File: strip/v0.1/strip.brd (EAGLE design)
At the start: 67 x 12 mm, 102 parts, among them IC1 LP2992, IC2 ADP3110A-SO8, IC3 MAX3051, IC4 OPA335, IC5 ADP3110A-SO8, IC6 ADP3110A-SO8, IC7 STM32F050CX, Q1 IRF7828, Q2 IRF7828, Q3 IRF7828, Q4 IRF7828, Q5 IRF7828, Q6 IRF7828

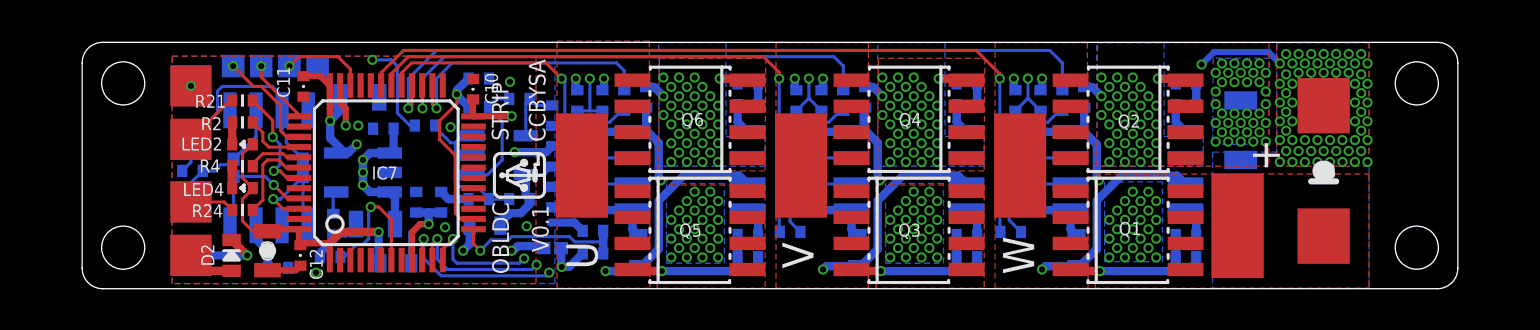
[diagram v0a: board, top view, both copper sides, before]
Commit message: Added tabs for panelization.
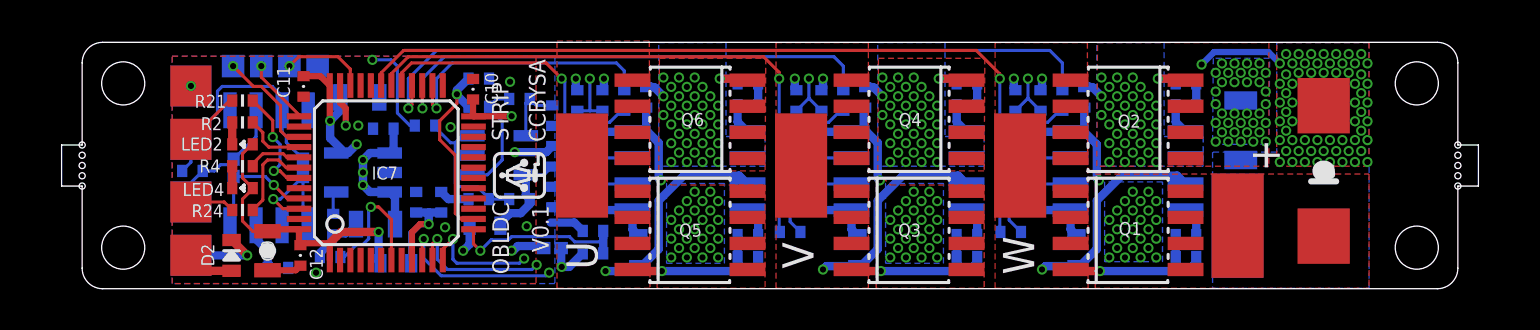
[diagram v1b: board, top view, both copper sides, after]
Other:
- board size 67 x 12 mm -> 69 x 12 mm
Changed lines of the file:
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@@
 <setting verticaltext="up"/>
 </settings>
-<grid distance="3" unitdist="mil" unit="mm" style="dots" multiple="1" display="yes" altdistance="0.5" altunitdist="mil" altunit="mil"/>
+<grid distance="0.5" unitdist="mm" unit="mm" style="dots" multiple="1" display="yes" altdistance="0.5" altunitdist="mil" altunit="mil"/>
 <layers>
 <layer number="1" name="Top" color="4" fill="1" visible="yes" active="yes"/>
@@
 <layer number="43" name="vRestrict" color="2" fill="10" visible="no" active="yes"/>
 <layer number="44" name="Drills" color="7" fill="1" visible="no" active="yes"/>
-<layer number="45" name="Holes" color="7" fill="1" visible="no" active="yes"/>
+<layer number="45" name="Holes" color="7" fill="1" visible="yes" active="yes"/>
 <layer number="46" name="Milling" color="3" fill="1" visible="no" active="yes"/>
 <layer number="47" name="Measures" color="7" fill="1" visible="no" active="yes"/>
@@
 <wire x1="-3" y1="0" x2="62" y2="0" width="0" layer="20"/>
 <wire x1="62" y1="0" x2="63" y2="1" width="0" layer="20" curve="90"/>
-<wire x1="63" y1="1" x2="63" y2="11" width="0" layer="20"/>
+<wire x1="63" y1="1" x2="63" y2="5" width="0" layer="20"/>
+<wire x1="63" y1="5" x2="64" y2="5" width="0" layer="20"/>
+<wire x1="64" y1="5" x2="64" y2="7" width="0" layer="20"/>
+<wire x1="64" y1="7" x2="63" y2="7" width="0" layer="20"/>
+<wire x1="63" y1="7" x2="63" y2="11" width="0" layer="20"/>
 <wire x1="63" y1="11" x2="62" y2="12" width="0" layer="20" curve="90"/>
 <wire x1="62" y1="12" x2="-3" y2="12" width="0" layer="20"/>
 <wire x1="-3" y1="12" x2="-4" y2="11" width="0" layer="20" curve="90"/>
-<wire x1="-4" y1="11" x2="-4" y2="1" width="0" layer="20"/>
+<wire x1="-4" y1="11" x2="-4" y2="7" width="0" layer="20"/>
+<wire x1="-4" y1="7" x2="-5" y2="7" width="0" layer="20"/>
+<wire x1="-5" y1="7" x2="-5" y2="5" width="0" layer="20"/>
+<wire x1="-5" y1="5" x2="-4" y2="5" width="0" layer="20"/>
+<wire x1="-4" y1="5" x2="-4" y2="1" width="0" layer="20"/>
 <text x="57.8104" y="4.441" size="0.8128" layer="22" font="vector" ratio="19" rot="MR90" align="bottom-center">OBLDC</text>
 <text x="54.102" y="4.5172" size="0.8128" layer="22" font="vector" ratio="19" rot="MR90" align="bottom-center">STRIP</text>
@@
 <wire x1="0" y1="13" x2="0" y2="-1" width="0.1524" layer="102"/>
 <wire x1="59" y1="13" x2="59" y2="-1" width="0.1524" layer="102"/>
+<hole x="63" y="6.5" drill="0.3"/>
+<hole x="63" y="6" drill="0.3"/>
+<hole x="63" y="5.5" drill="0.3"/>
+<hole x="63" y="7" drill="0.3"/>
+<hole x="63" y="5" drill="0.3"/>
+<hole x="-4" y="5" drill="0.3"/>
+<hole x="-4" y="5.5" drill="0.3"/>
+<hole x="-4" y="6" drill="0.3"/>
+<hole x="-4" y="6.5" drill="0.3"/>
+<hole x="-4" y="7" drill="0.3"/>
 </plain>
 <attributes>
@@
 </signal>
 </signals>
-<errors>
-</errors>
 </board>
 </drawing>

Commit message: More work on the BOM and part documentation.
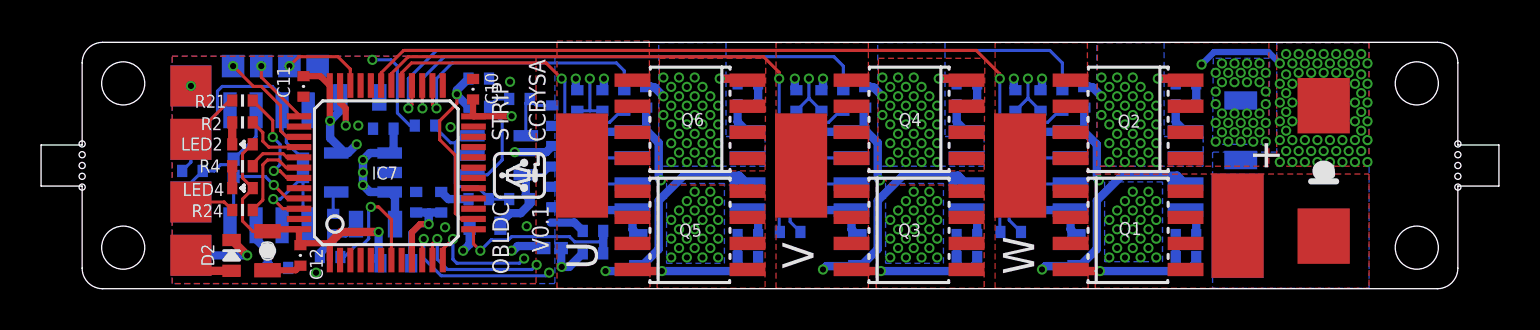
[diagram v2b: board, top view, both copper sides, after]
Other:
- board size 69 x 12 mm -> 71 x 12 mm
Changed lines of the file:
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@@
 <setting verticaltext="up"/>
 </settings>
-<grid distance="0.5" unitdist="mm" unit="mm" style="dots" multiple="1" display="yes" altdistance="0.5" altunitdist="mil" altunit="mil"/>
+<grid distance="1" unitdist="mil" unit="mil" style="dots" multiple="1" display="yes" altdistance="0.5" altunitdist="mil" altunit="mil"/>
 <layers>
 <layer number="1" name="Top" color="4" fill="1" visible="yes" active="yes"/>
@@
 <layer number="43" name="vRestrict" color="2" fill="10" visible="no" active="yes"/>
 <layer number="44" name="Drills" color="7" fill="1" visible="no" active="yes"/>
-<layer number="45" name="Holes" color="7" fill="1" visible="yes" active="yes"/>
+<layer number="45" name="Holes" color="7" fill="1" visible="no" active="yes"/>
 <layer number="46" name="Milling" color="3" fill="1" visible="no" active="yes"/>
 <layer number="47" name="Measures" color="7" fill="1" visible="no" active="yes"/>
@@
 <layer number="100" name="Muster" color="7" fill="1" visible="no" active="no"/>
 <layer number="101" name="Patch_Top" color="12" fill="4" visible="no" active="yes"/>
-<layer number="102" name="Vscore" color="7" fill="1" visible="yes" active="yes"/>
+<layer number="102" name="Vscore" color="7" fill="1" visible="no" active="yes"/>
 <layer number="103" name="origins2" color="7" fill="1" visible="no" active="yes"/>
 <layer number="104" name="Name" color="7" fill="1" visible="no" active="yes"/>
@@
 <wire x1="62" y1="0" x2="63" y2="1" width="0" layer="20" curve="90"/>
 <wire x1="63" y1="1" x2="63" y2="5" width="0" layer="20"/>
-<wire x1="63" y1="5" x2="64" y2="5" width="0" layer="20"/>
-<wire x1="64" y1="5" x2="64" y2="7" width="0" layer="20"/>
-<wire x1="64" y1="7" x2="63" y2="7" width="0" layer="20"/>
+<wire x1="63" y1="5" x2="65" y2="5" width="0" layer="20"/>
+<wire x1="65" y1="5" x2="65" y2="7" width="0" layer="20"/>
+<wire x1="65" y1="7" x2="63" y2="7" width="0" layer="20"/>
 <wire x1="63" y1="7" x2="63" y2="11" width="0" layer="20"/>
 <wire x1="63" y1="11" x2="62" y2="12" width="0" layer="20" curve="90"/>
@@
 <wire x1="-3" y1="12" x2="-4" y2="11" width="0" layer="20" curve="90"/>
 <wire x1="-4" y1="11" x2="-4" y2="7" width="0" layer="20"/>
-<wire x1="-4" y1="7" x2="-5" y2="7" width="0" layer="20"/>
-<wire x1="-5" y1="7" x2="-5" y2="5" width="0" layer="20"/>
-<wire x1="-5" y1="5" x2="-4" y2="5" width="0" layer="20"/>
+<wire x1="-4" y1="7" x2="-6" y2="7" width="0" layer="20"/>
+<wire x1="-6" y1="7" x2="-6" y2="5" width="0" layer="20"/>
+<wire x1="-6" y1="5" x2="-4" y2="5" width="0" layer="20"/>
 <wire x1="-4" y1="5" x2="-4" y2="1" width="0" layer="20"/>
 <text x="57.8104" y="4.441" size="0.8128" layer="22" font="vector" ratio="19" rot="MR90" align="bottom-center">OBLDC</text>
@@
 <wire x1="0" y1="13" x2="0" y2="-1" width="0.1524" layer="102"/>
 <wire x1="59" y1="13" x2="59" y2="-1" width="0.1524" layer="102"/>
-<hole x="63" y="6.5" drill="0.3"/>
+<hole x="63" y="6.5254" drill="0.3"/>
 <hole x="63" y="6" drill="0.3"/>
-<hole x="63" y="5.5" drill="0.3"/>
-<hole x="63" y="7" drill="0.3"/>
-<hole x="63" y="5" drill="0.3"/>
-<hole x="-4" y="5" drill="0.3"/>
-<hole x="-4" y="5.5" drill="0.3"/>
+<hole x="63" y="5.4746" drill="0.3"/>
+<hole x="63" y="7.0508" drill="0.3"/>
+<hole x="63" y="4.9492" drill="0.3"/>
+<hole x="-4" y="4.9492" drill="0.3"/>
+<hole x="-4" y="5.4746" drill="0.3"/>
 <hole x="-4" y="6" drill="0.3"/>
-<hole x="-4" y="6.5" drill="0.3"/>
-<hole x="-4" y="7" drill="0.3"/>
+<hole x="-4" y="6.5254" drill="0.3"/>
+<hole x="-4" y="7.0508" drill="0.3"/>
 </plain>
 <attributes>
@@
 <attribute name="NAME" x="48.8442" y="2.3074" size="0.635" layer="26" font="vector" ratio="16" rot="MR0"/>
 <attribute name="VALUE" x="50.9016" y="1.3168" size="0.635" layer="28" font="vector" ratio="16" rot="MR0"/>
-<attribute name="PARTNO" value="*" x="49.7586" y="2.6122" size="1.778" layer="28" rot="MR0" display="off"/>
+<attribute name="PARTNO" value="res-0402-0" x="49.7586" y="2.6122" size="1.778" layer="28" rot="MR0" display="off"/>
 </element>
 <element name="L3" library="pel_dipol_comp" package="0402-IND" value="" x="49.7586" y="8.9368" smashed="yes" rot="MR180">
 <attribute name="NAME" x="48.8442" y="8.632" size="0.635" layer="26" font="vector" ratio="16" rot="MR0"/>
 <attribute name="VALUE" x="48.6156" y="10.2322" size="0.635" layer="28" font="vector" ratio="16" rot="MR180"/>
-<attribute name="PARTNO" value="*" x="49.7586" y="8.9368" size="1.778" layer="28" rot="MR180" display="off"/>
+<attribute name="PARTNO" value="res-0402-0" x="49.7586" y="8.9368" size="1.778" layer="28" rot="MR180" display="off"/>
 </element>
 <element name="L4" library="pel_dipol_comp" package="0402-IND" value="" x="39.0906" y="2.6122" smashed="yes" rot="MR0">
 <attribute name="NAME" x="38.2524" y="2.3074" size="0.635" layer="26" font="vector" ratio="16" rot="MR0"/>
 <attribute name="VALUE" x="40.2336" y="1.3168" size="0.635" layer="28" font="vector" ratio="16" rot="MR0"/>
-<attribute name="PARTNO" value="*" x="39.0906" y="2.6122" size="1.778" layer="28" rot="MR0" display="off"/>
+<attribute name="PARTNO" value="res-0402-0" x="39.0906" y="2.6122" size="1.778" layer="28" rot="MR0" display="off"/>
 </element>
 <element name="L5" library="pel_dipol_comp" package="0402-IND" value="" x="39.0906" y="8.9368" smashed="yes" rot="MR180">
 <attribute name="NAME" x="38.2524" y="8.5558" size="0.635" layer="26" font="vector" ratio="16" rot="MR0"/>
 <attribute name="VALUE" x="37.9476" y="10.2322" size="0.635" layer="28" font="vector" ratio="16" rot="MR180"/>
-<attribute name="PARTNO" value="*" x="39.0906" y="8.9368" size="1.778" layer="28" rot="MR180" display="off"/>
+<attribute name="PARTNO" value="res-0402-0" x="39.0906" y="8.9368" size="1.778" layer="28" rot="MR180" display="off"/>
 </element>
 <element name="L6" library="pel_dipol_comp" package="0402-IND" value="" x="28.4226" y="2.6122" smashed="yes" rot="MR0">
 <attribute name="NAME" x="27.5844" y="2.3074" size="0.635" layer="26" font="vector" ratio="16" rot="MR0"/>
 <attribute name="VALUE" x="29.5656" y="1.3168" size="0.635" layer="28" font="vector" ratio="16" rot="MR0"/>
-<attribute name="PARTNO" value="*" x="28.4226" y="2.6122" size="1.778" layer="28" rot="MR0" display="off"/>
+<attribute name="PARTNO" value="res-0402-0" x="28.4226" y="2.6122" size="1.778" layer="28" rot="MR0" display="off"/>
 </element>
 <element name="L7" library="pel_dipol_comp" package="0402-IND" value="" x="28.4226" y="8.9368" smashed="yes" rot="MR180">
 <attribute name="NAME" x="27.5844" y="8.632" size="0.635" layer="26" font="vector" ratio="16" rot="MR0"/>
 <attribute name="VALUE" x="27.2796" y="10.2322" size="0.635" layer="28" font="vector" ratio="16" rot="MR180"/>
-<attribute name="PARTNO" value="*" x="28.4226" y="8.9368" size="1.778" layer="28" rot="MR180" display="off"/>
+<attribute name="PARTNO" value="res-0402-0" x="28.4226" y="8.9368" size="1.778" layer="28" rot="MR180" display="off"/>
 </element>
 <element name="Q1" library="open-bldc" package="SO8" value="IRF7828" x="46.9392" y="2.8408" smashed="yes" rot="R270">
@@
 <element name="C13" library="pel_dipol_comp" package="0402-CAP" value="100n" x="5.5372" y="1.012" rot="MR0">
 <attribute name="PARTNO" value="cap-cer-0402-100n" x="12.7762" y="17.8522" size="1.778" layer="28" rot="MR0" display="off"/>
+<attribute name="DNP" value="T" x="5.5372" y="1.012" size="1.778" layer="28" rot="MR0" display="off"/>
 </element>
 <element name="R59" library="pel_dipol_comp" package="0402-RES" value="120R/DNP" x="1.3716" y="5.7364" rot="MR180">
 <attribute name="PARTNO" value="res-0402-60.4" x="-7.4676" y="6.8032" size="1.778" layer="28" rot="MR180" display="off"/>
-</element>
-<element name="IC3" library="open-bldc" package="SO8" value="MAX3051" x="5.1054" y="5.8888" rot="MR0"/>
-<element name="J1" library="pel_jumpers" package="0402-SQJMP" value="" x="3.3782" y="5.8888" rot="MR90"/>
-<element name="J2" library="pel_jumpers" package="0402-SQJMP" value="" x="6.7564" y="5.8888" rot="MR90"/>
-<element name="J3" library="pel_jumpers" package="0402-SQJMP" value="" x="18.9042" y="1.9776" rot="MR180"/>
+<attribute name="DNP" value="T" x="1.3716" y="5.7364" size="1.778" layer="28" rot="MR180" display="off"/>
+</element>
+<element name="IC3" library="open-bldc" package="SO8" value="MAX3051" x="5.1054" y="5.8888" rot="MR0">
+<attribute name="DNP" value="T" x="5.1054" y="5.8888" size="1.778" layer="28" rot="MR0" display="off"/>
+<attribute name="PARTNO" value="*" x="5.1054" y="5.8888" size="1.778" layer="28" rot="MR0" display="off"/>
+</element>
+<element name="J1" library="pel_jumpers" package="0402-SQJMP" value="" x="3.3782" y="5.8888" rot="MR90">
+<attribute name="PARTNO" value="res-0402-0" x="3.3782" y="5.8888" size="1.778" layer="28" rot="MR90" display="off"/>
+</element>
+<element name="J2" library="pel_jumpers" package="0402-SQJMP" value="" x="6.7564" y="5.8888" rot="MR90">
+<attribute name="PARTNO" value="res-0402-0" x="6.7564" y="5.8888" size="1.778" layer="28" rot="MR90" display="off"/>
+</element>
+<element name="J3" library="pel_jumpers" package="0402-SQJMP" value="" x="18.9042" y="1.9776" rot="MR180">
+<attribute name="PARTNO" value="res-0402-0" x="18.9042" y="1.9776" size="1.778" layer="28" rot="MR180" display="off"/>
+</element>
 </elements>
 <signals>
